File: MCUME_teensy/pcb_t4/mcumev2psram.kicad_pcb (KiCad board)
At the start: 2 copper layers, 72.4 x 101.6 mm, 0 parts

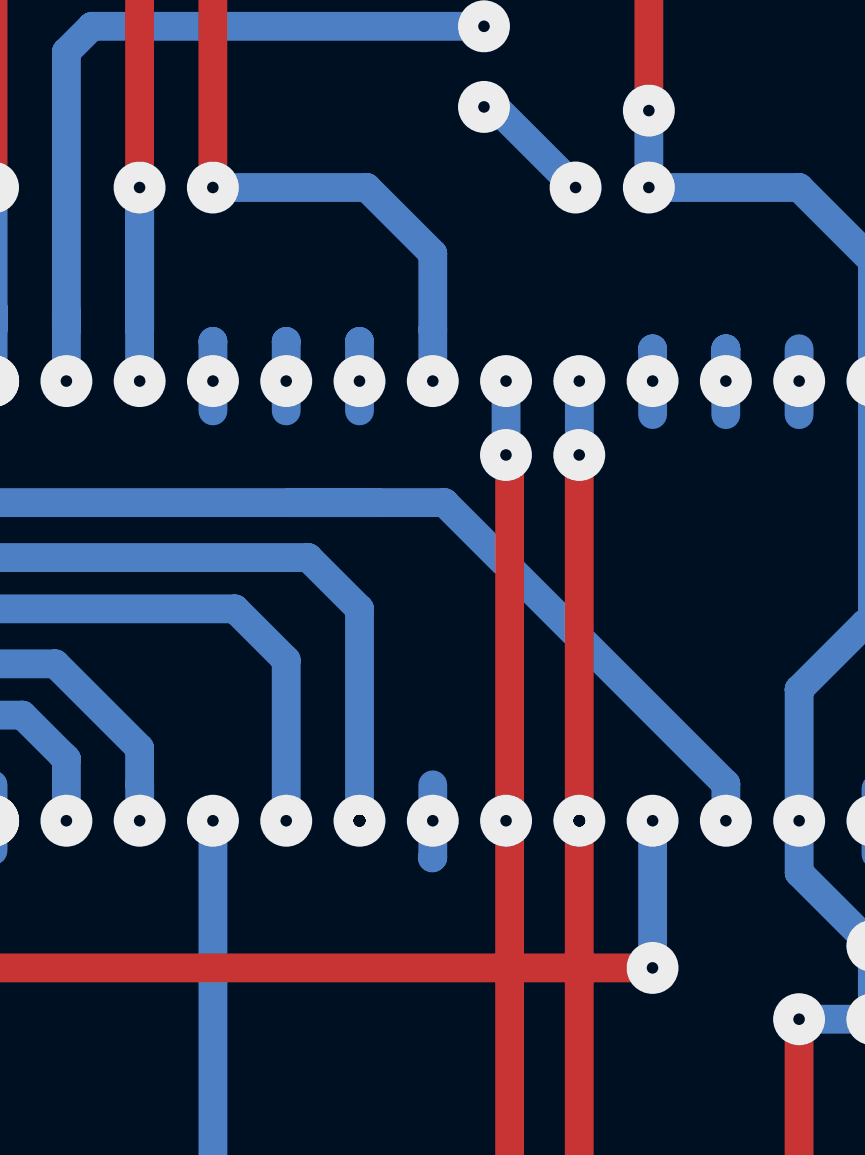
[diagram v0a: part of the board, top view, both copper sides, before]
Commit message: add support for 320x240 st7789 display
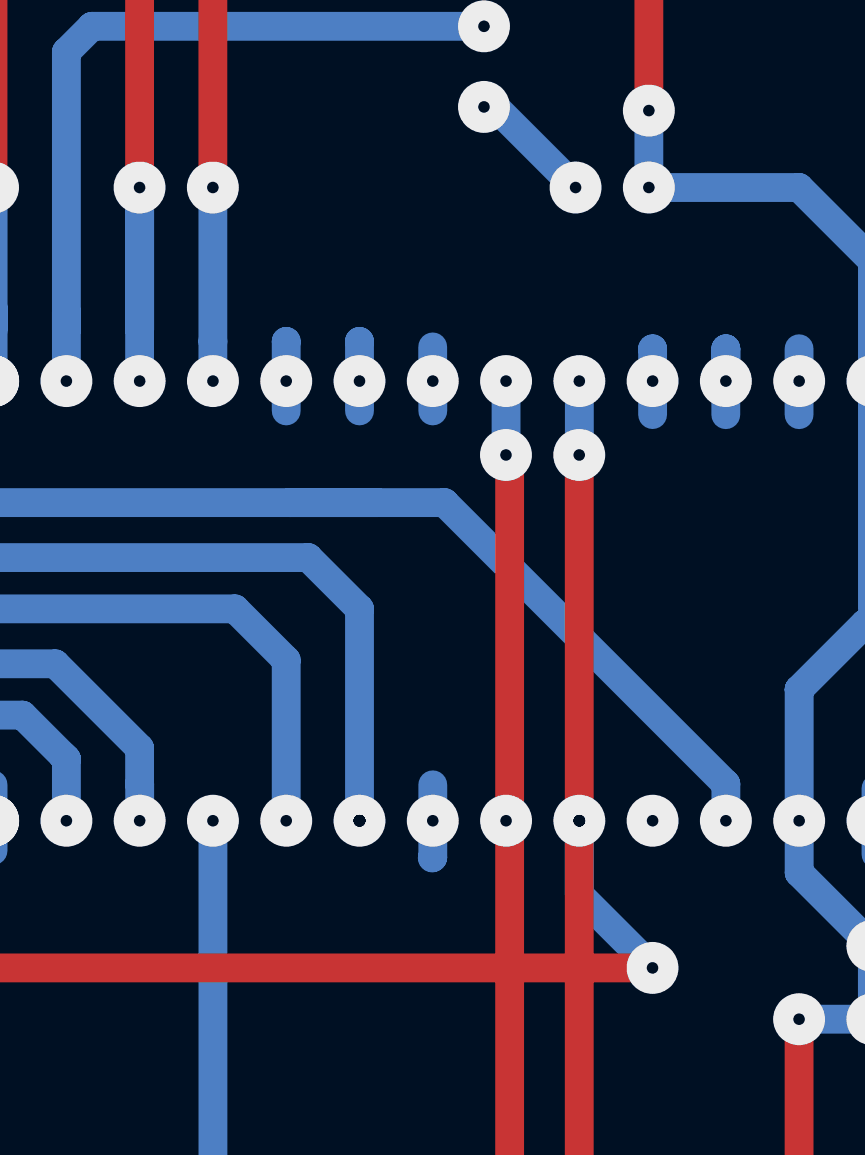
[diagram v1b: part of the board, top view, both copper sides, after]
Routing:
- net (no net): track 1541.4 -> 1536.0 mm
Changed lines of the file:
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@@
     (thickness 1.6)
     (drawings 5)
-    (tracks 360)
+    (tracks 361)
     (zones 0)
     (modules 0)
@@
   (via (at 213.741 53.213) (size 0.8) (drill 0.4) (layers F.Cu B.Cu) (net 0))
   (via (at 213.741 53.213) (size 1.8) (drill 0.4) (layers F.Cu B.Cu) (net 0))
-  (via (at 181.739941 85.957485) (size 1.8) (drill 0.4) (layers F.Cu B.Cu) (net 0) (status 1000000))
+  (via (at 181.739941 85.957485) (size 1.8) (drill 0.4) (layers F.Cu B.Cu) (net 0))
   (via (at 184.279941 85.957485) (size 1.8) (drill 0.4) (layers F.Cu B.Cu) (net 0))
   (via (at 186.819941 85.957485) (size 1.8) (drill 0.4) (layers F.Cu B.Cu) (net 0))
@@
   (segment (start 189.359941 64.010941) (end 189.357 64.008) (width 1) (layer B.Cu) (net 0))
   (segment (start 189.359941 68.939485) (end 189.359941 64.010941) (width 1) (layer B.Cu) (net 0))
-  (segment (start 199.519941 68.939485) (end 199.519941 66.296941) (width 1) (layer B.Cu) (net 0))
-  (segment (start 197.231 64.008) (end 199.519941 66.296941) (width 1) (layer B.Cu) (net 0))
-  (segment (start 191.897 64.008) (end 197.231 64.008) (width 1) (layer B.Cu) (net 0))
   (segment (start 176.53 43.053) (end 176.53 64.008) (width 1) (layer F.Cu) (net 0))
   (via (at 176.53 88.392) (size 1.8) (drill 0.4) (layers F.Cu B.Cu) (net 0))
@@
   (via (at 207.137 91.059) (size 1.8) (drill 0.4) (layers F.Cu B.Cu) (net 0))
   (segment (start 207.139941 91.056059) (end 207.137 91.059) (width 1) (layer B.Cu) (net 0))
-  (segment (start 207.139941 85.957485) (end 207.139941 91.056059) (width 1) (layer B.Cu) (net 0))
   (segment (start 176.53 88.392) (end 176.53 91.059) (width 1) (layer B.Cu) (net 0))
   (segment (start 176.53 91.059) (end 207.137 91.059) (width 1) (layer F.Cu) (net 0))
@@
   (segment (start 179.07 66.548) (end 179.07 85.979) (width 1) (layer F.Cu) (net 0))
   (segment (start 176.53 66.548) (end 176.53 88.392) (width 1) (layer F.Cu) (net 0))
-  (segment (start 199.519941 68.939485) (end 199.519941 70.717485) (width 1) (layer B.Cu) (net 0))
   (segment (start 189.357 70.714544) (end 189.359941 70.717485) (width 1) (layer B.Cu) (net 0))
   (segment (start 189.357 64.008) (end 189.357 70.714544) (width 1) (layer B.Cu) (net 0))
@@
   (segment (start 194.439941 69.344941) (end 194.439941 71.752059) (width 1) (layer B.Cu) (net 0))
   (segment (start 194.437 69.342) (end 194.439941 69.344941) (width 1) (layer B.Cu) (net 0))
-  (segment (start 191.899941 69.344941) (end 191.899941 71.752059) (width 1) (layer B.Cu) (net 0))
   (segment (start 191.897 69.342) (end 191.899941 69.344941) (width 1) (layer B.Cu) (net 0))
   (segment (start 208.026 118.237) (end 214.884 118.237) (width 1) (layer B.Cu) (net 0))
@@
   (segment (start 146.812 94.615) (end 146.812 125.857) (width 1) (layer B.Cu) (net 0))
   (segment (start 148.717 92.71) (end 146.812 94.615) (width 1) (layer B.Cu) (net 0))
+  (segment (start 199.517 70.714544) (end 199.519941 70.717485) (width 1) (layer B.Cu) (net 0))
+  (segment (start 199.517 69.5325) (end 199.517 70.714544) (width 1) (layer B.Cu) (net 0))
+  (segment (start 199.519941 70.717485) (end 199.519941 71.752059) (width 1) (layer B.Cu) (net 0))
+  (segment (start 191.897 70.714544) (end 191.899941 70.717485) (width 1) (layer B.Cu) (net 0))
+  (segment (start 191.897 64.008) (end 191.897 70.714544) (width 1) (layer B.Cu) (net 0))
+  (segment (start 204.599941 88.521941) (end 204.599941 85.957485) (width 1) (layer B.Cu) (net 0))
+  (segment (start 207.137 91.059) (end 204.599941 88.521941) (width 1) (layer B.Cu) (net 0))
 )
